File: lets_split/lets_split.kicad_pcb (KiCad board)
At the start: 2 copper layers, 112 x 79 mm, 62 parts, among them J1 3PIN, J2 6PIN, J3 3PIN, SW1 SW_PUSH, SW10 SW_PUSH, SW11 SW_PUSH, SW12 SW_PUSH, SW13 SW_PUSH, SW14 SW_PUSH, SW15 SW_PUSH, SW16 SW_PUSH, SW17 SW_PUSH, SW18 SW_PUSH, SW19 SW_PUSH, SW2 SW_PUSH, SW21 SW_PUSH, SW22 SW_PUSH, SW23 SW_PUSH, SW3 SW_PUSH, SW4 SW_PUSH, SW5 SW_PUSH, SW6 SW_PUSH, SW7 SW_PUSH, SW8 SW_PUSH, SW9 SW_PUSH, U2 HOLE, U3 HOLE, U4 HOLE, U5 HOLE

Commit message: Delete Lupine
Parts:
- removed G*** (x2): LOGO, LOGO
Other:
- board text added: "modified by mukko"

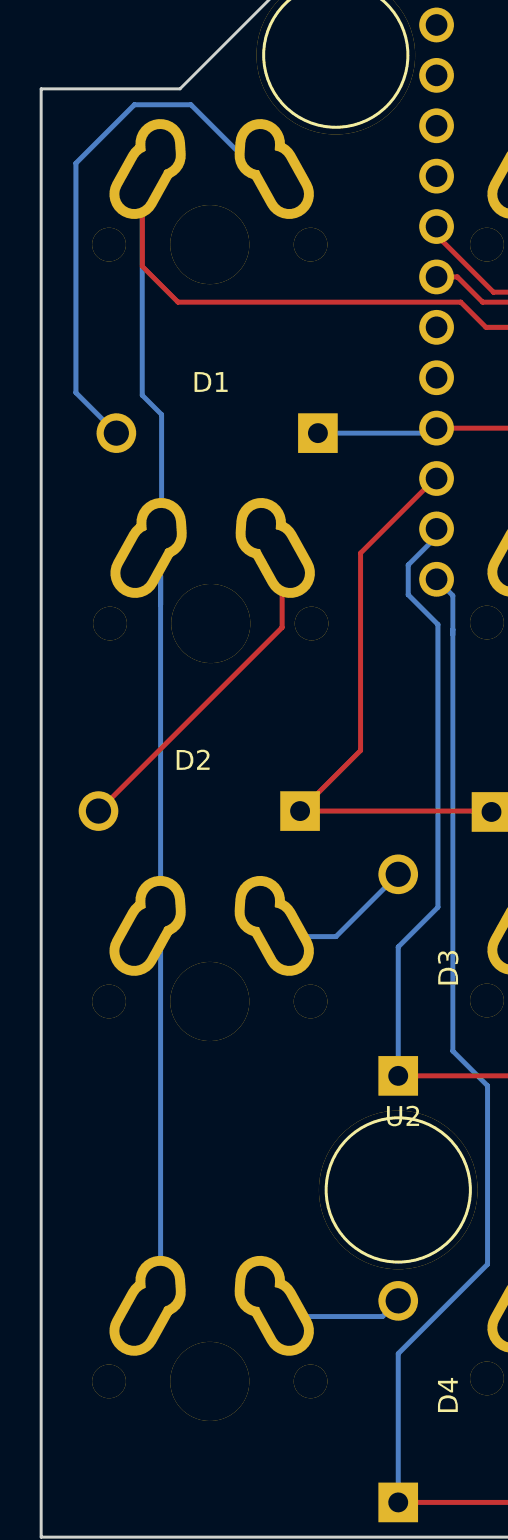
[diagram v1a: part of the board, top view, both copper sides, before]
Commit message: Fix alignments at left column
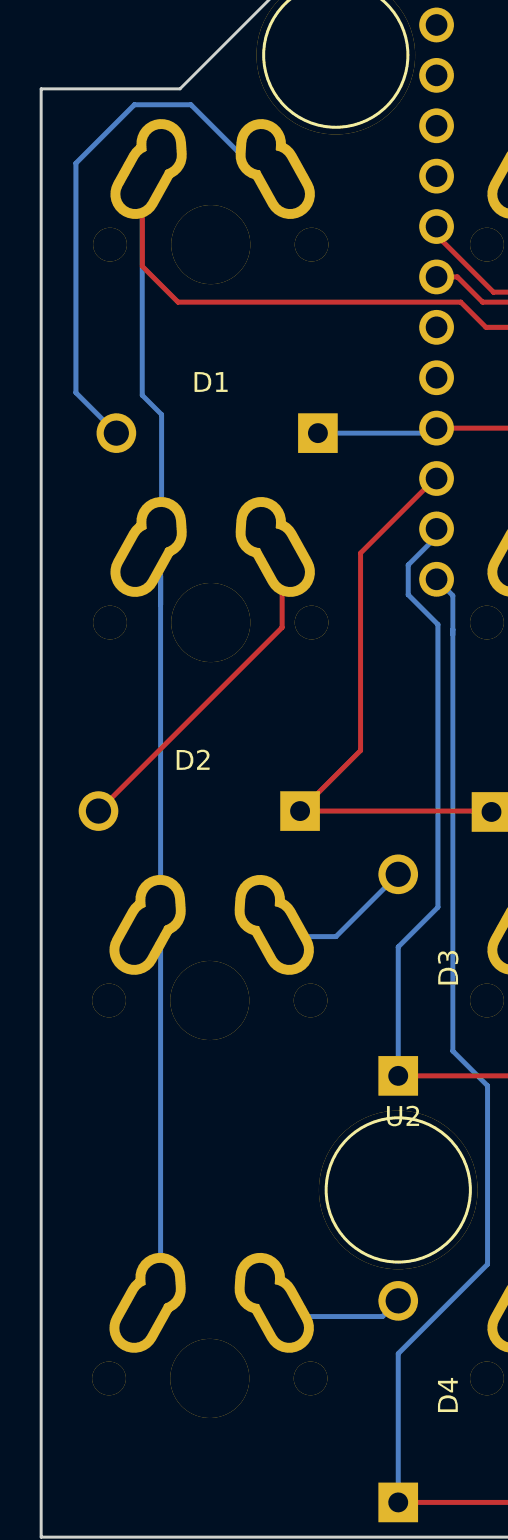
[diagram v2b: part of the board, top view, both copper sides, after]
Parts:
- moved SW4 0.15 mm to (45.5, 104.0)
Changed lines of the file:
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@@
   )
   (module flipalps:MXALPS_FLIP (layer F.Cu)
-    (at 45.5 46.85)
+    (at 45.55 46.85)
     (descr MXALPS)
     (tags MXALPS)
@@
       (effects (font (size 1.524 1.524) (thickness 0.3048)) (justify mirror))
     )
-    (fp_line (start -7.75 6.4) (end -7.75 -6.4) (layer Dwgs.User) (width 0.3))
-    (fp_line (start -7.75 6.4) (end 7.75 6.4) (layer Dwgs.User) (width 0.3))
-    (fp_line (start 7.75 6.4) (end 7.75 -6.4) (layer Dwgs.User) (width 0.3))
-    (fp_line (start 7.75 -6.4) (end -7.75 -6.4) (layer Dwgs.User) (width 0.3))
-    (fp_line (start -7.62 -7.62) (end 7.62 -7.62) (layer Dwgs.User) (width 0.3))
-    (fp_line (start 7.62 -7.62) (end 7.62 7.62) (layer Dwgs.User) (width 0.3))
-    (fp_line (start 7.62 7.62) (end -7.62 7.62) (layer Dwgs.User) (width 0.3))
-    (fp_line (start -7.62 7.62) (end -7.62 -7.62) (layer Dwgs.User) (width 0.3))
-    (pad 1 thru_hole oval (at -2.48 -4.79 3.9) (size 2.5 3.08) (drill oval 1.5 2.08) (layers *.Cu *.Mask F.SilkS)
+    (fp_line (start -7.62 7.62) (end -7.62 -7.62) (layer Dwgs.User) (width 0.3))
+    (fp_line (start 7.62 7.62) (end -7.62 7.62) (layer Dwgs.User) (width 0.3))
+    (fp_line (start 7.62 -7.62) (end 7.62 7.62) (layer Dwgs.User) (width 0.3))
+    (fp_line (start -7.62 -7.62) (end 7.62 -7.62) (layer Dwgs.User) (width 0.3))
+    (fp_line (start 7.75 -6.4) (end -7.75 -6.4) (layer Dwgs.User) (width 0.3))
+    (fp_line (start 7.75 6.4) (end 7.75 -6.4) (layer Dwgs.User) (width 0.3))
+    (fp_line (start -7.75 6.4) (end 7.75 6.4) (layer Dwgs.User) (width 0.3))
+    (fp_line (start -7.75 6.4) (end -7.75 -6.4) (layer Dwgs.User) (width 0.3))
+    (pad 2 thru_hole oval (at 2.52 -4.79 356.1) (size 2.5 3.08) (drill oval 1.5 2.08) (layers *.Cu *.Mask F.SilkS)
+      (net 1 "Net-(D1-Pad2)"))
+    (pad 1 thru_hole oval (at -3.405 -3.27 330.95) (size 2.5 4.17) (drill oval 1.5 3.17) (layers *.Cu *.Mask F.SilkS)
       (net 36 col0))
+    (pad "" np_thru_hole circle (at 5.08 0) (size 1.70181 1.70181) (drill 1.7018) (layers *.Cu *.Mask F.SilkS)
+      (clearance 0.1524))
+    (pad "" np_thru_hole circle (at -5.08 0) (size 1.70181 1.70181) (drill 1.7018) (layers *.Cu *.Mask F.SilkS)
+      (clearance 0.1524))
+    (pad "" np_thru_hole circle (at 0 0) (size 3.98781 3.98781) (drill 3.9878) (layers *.Cu *.Mask F.SilkS)
+      (clearance 0.1524))
     (pad 2 thru_hole oval (at 3.595 -3.27 29) (size 2.5 4.17) (drill oval 1.5 3.17) (layers *.Cu *.Mask F.SilkS)
       (net 1 "Net-(D1-Pad2)"))
-    (pad "" np_thru_hole circle (at 0 0) (size 3.98781 3.98781) (drill 3.9878) (layers *.Cu *.Mask F.SilkS)
-      (clearance 0.1524))
-    (pad "" np_thru_hole circle (at -5.08 0) (size 1.70181 1.70181) (drill 1.7018) (layers *.Cu *.Mask F.SilkS)
-      (clearance 0.1524))
-    (pad "" np_thru_hole circle (at 5.08 0) (size 1.70181 1.70181) (drill 1.7018) (layers *.Cu *.Mask F.SilkS)
-      (clearance 0.1524))
-    (pad 1 thru_hole oval (at -3.405 -3.27 330.95) (size 2.5 4.17) (drill oval 1.5 3.17) (layers *.Cu *.Mask F.SilkS)
+    (pad 1 thru_hole oval (at -2.48 -4.79 3.9) (size 2.5 3.08) (drill oval 1.5 2.08) (layers *.Cu *.Mask F.SilkS)
       (net 36 col0))
-    (pad 2 thru_hole oval (at 2.52 -4.79 356.1) (size 2.5 3.08) (drill oval 1.5 2.08) (layers *.Cu *.Mask F.SilkS)
-      (net 1 "Net-(D1-Pad2)"))
-  )
-  (module flipalps:MXALPS_FLIP (layer F.Cu)
-    (at 45.55 65.95)
+  )
+  (module flipalps:MXALPS_FLIP (layer F.Cu)
+    (at 45.55 65.9)
     (descr MXALPS)
     (tags MXALPS)
@@
   )
   (module flipalps:MXALPS_FLIP (layer F.Cu)
-    (at 45.5 85)
+    (at 45.5 84.95)
     (descr MXALPS)
     (tags MXALPS)
@@
   )
   (module flipalps:MXALPS_FLIP (layer F.Cu)
-    (at 45.5 104.15)
+    (at 45.5 104)
     (descr MXALPS)
     (tags MXALPS)
@@
         (xy 80.5 38.5) (xy 121.5 38.5) (xy 125.75 34.25) (xy 138 34.25) (xy 142.75 39)
         (xy 149 39) (xy 149 112) (xy 37 112) (xy 37 39) (xy 44 39)
-        (xy 50 33) (xy 75 33) (xy 80.5 38.5)
+        (xy 50 33) (xy 75 33)
       )
     )
@@
         (xy 80.5 38.5) (xy 121.5 38.5) (xy 125.75 34.25) (xy 138 34.25) (xy 142.75 39)
         (xy 149 39) (xy 149 112) (xy 37 112) (xy 37 39) (xy 44 39)
-        (xy 50 33) (xy 75 33) (xy 80.5 38.5)
+        (xy 50 33) (xy 75 33)
       )
     )
